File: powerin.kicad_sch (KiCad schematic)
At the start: 12 parts, among them U5 TPS2592xx

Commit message: Add optional ESP32-C3 WiFi sheet, convert hand-solder parts to through-hole
- New wifi sheet: ESP32-C3-MINI-1 module on SPI to spare FPGA bank 34, with EN/boot-strap networks, 3V3 bypass/bulk caps and a UART debug header
- Replace SMD hand-solder resistors, LEDs, zener, fuse and ceramic caps with THT equivalents; bulk 10uF/22uF caps become polarized electrolytics
- Fill in LCSC part numbers for the new parts and regenerate BOM and ERC report
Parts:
- C21: footprint Capacitor_SMD:C_0805_2012Metric_Pad1.18x1.45mm_HandSolder -> Capacitor_THT:CP_Radial_D5.0mm_P2.00mm; symbol Device:C -> Device:C_Polarized; LCSC Part (none) -> C47344176
- C22: footprint Capacitor_SMD:C_0603_1608Metric_Pad1.08x0.95mm_HandSolder -> Capacitor_THT:C_Disc_D3.0mm_W2.0mm_P2.50mm; LCSC Part (none) -> C5632430
- C23: footprint Capacitor_SMD:C_0603_1608Metric_Pad1.08x0.95mm_HandSolder -> Capacitor_THT:C_Disc_D3.0mm_W2.0mm_P2.50mm; LCSC Part (none) -> C1624895
- D2: footprint Diode_SMD:D_SMB_Handsoldering -> Diode_THT:D_DO-41_SOD81_P10.16mm_Horizontal
- F1: footprint Fuse:Fuse_1812_4532Metric_Pad1.30x3.40mm_HandSolder -> easyeda:FUSE-TH_L9.5-W3.5-P5.08-D0.8-S1.2
- R13, R14, R15, R16: footprint Resistor_SMD:R_0603_1608Metric_Pad0.98x0.95mm_HandSolder -> Resistor_THT:R_Axial_DIN0207_L6.3mm_D2.5mm_P10.16mm_Horizontal
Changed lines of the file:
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@@
 			)
 		)
-		(property "Footprint" "Resistor_SMD:R_0603_1608Metric_Pad0.98x0.95mm_HandSolder"
+		(property "Footprint" "Resistor_THT:R_Axial_DIN0207_L6.3mm_D2.5mm_P10.16mm_Horizontal"
 			(at 135.89 31.242 90)
 			(hide yes)
@@
 			)
 		)
-		(property "Footprint" "Resistor_SMD:R_0603_1608Metric_Pad0.98x0.95mm_HandSolder"
+		(property "Footprint" "Resistor_THT:R_Axial_DIN0207_L6.3mm_D2.5mm_P10.16mm_Horizontal"
 			(at 273.812 50.8 90)
 			(hide yes)
@@
 	)
 	(symbol
-		(lib_id "Device:C")
+		(lib_id "Device:C_Polarized")
 		(at 181.61 36.83 0)
 		(unit 1)
@@
 			)
 		)
-		(property "Footprint" "Capacitor_SMD:C_0805_2012Metric_Pad1.18x1.45mm_HandSolder"
+		(property "Footprint" "Capacitor_THT:CP_Radial_D5.0mm_P2.00mm"
 			(at 182.5752 40.64 0)
 			(hide yes)
@@
 		(property "Description" "Unpolarized capacitor"
 			(at 181.61 36.83 0)
+			(hide yes)
+			(show_name no)
+			(do_not_autoplace no)
+			(effects
+				(font
+					(size 1.27 1.27)
+				)
+			)
+		)
+		(property "LCSC Part" "C47344176"
+			(at 0 0 0)
 			(hide yes)
 			(show_name no)
@@
 			)
 		)
-		(property "Footprint" "Capacitor_SMD:C_0603_1608Metric_Pad1.08x0.95mm_HandSolder"
+		(property "Footprint" "Capacitor_THT:C_Disc_D3.0mm_W2.0mm_P2.50mm"
 			(at 266.3952 54.61 0)
 			(hide yes)
@@
 		(property "Description" "Unpolarized capacitor"
 			(at 265.43 50.8 0)
+			(hide yes)
+			(show_name no)
+			(do_not_autoplace no)
+			(effects
+				(font
+					(size 1.27 1.27)
+				)
+			)
+		)
+		(property "LCSC Part" "C1624895"
+			(at 0 0 0)
 			(hide yes)
 			(show_name no)
@@
 			)
 		)
-		(property "Footprint" "Capacitor_SMD:C_0603_1608Metric_Pad1.08x0.95mm_HandSolder"
+		(property "Footprint" "Capacitor_THT:C_Disc_D3.0mm_W2.0mm_P2.50mm"
 			(at 194.0052 40.64 0)
 			(hide yes)
@@
 		(property "Description" "Unpolarized capacitor"
 			(at 193.04 36.83 0)
+			(hide yes)
+			(show_name no)
+			(do_not_autoplace no)
+			(effects
+				(font
+					(size 1.27 1.27)
+				)
+			)
+		)
+		(property "LCSC Part" "C5632430"
+			(at 0 0 0)
 			(hide yes)
 			(show_name no)
@@
 			)
 		)
-		(property "Footprint" "Diode_SMD:D_SMB_Handsoldering"
+		(property "Footprint" "Diode_THT:D_DO-41_SOD81_P10.16mm_Horizontal"
 			(at 44.45 35.56 0)
 			(hide yes)
@@
 			)
 		)
-		(property "Footprint" "Fuse:Fuse_1812_4532Metric_Pad1.30x3.40mm_HandSolder"
+		(property "Footprint" "easyeda:FUSE-TH_L9.5-W3.5-P5.08-D0.8-S1.2"
 			(at 49.53 27.94 0)
 			(hide yes)
@@
 			)
 		)
-		(property "Footprint" "Resistor_SMD:R_0603_1608Metric_Pad0.98x0.95mm_HandSolder"
+		(property "Footprint" "Resistor_THT:R_Axial_DIN0207_L6.3mm_D2.5mm_P10.16mm_Horizontal"
 			(at 135.89 28.702 90)
 			(hide yes)
@@
 			)
 		)
-		(property "Footprint" "Resistor_SMD:R_0603_1608Metric_Pad0.98x0.95mm_HandSolder"
+		(property "Footprint" "Resistor_THT:R_Axial_DIN0207_L6.3mm_D2.5mm_P10.16mm_Horizontal"
 			(at 239.268 38.1 90)
 			(hide yes)

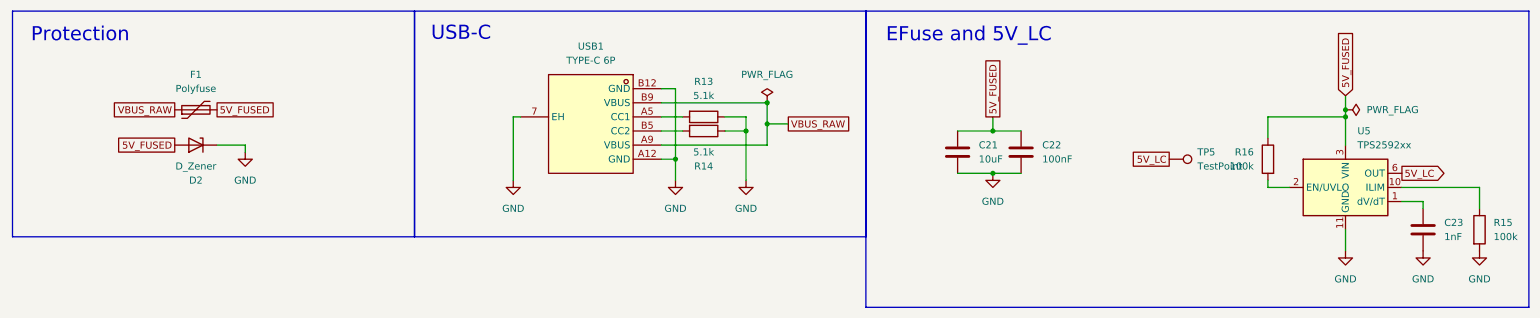
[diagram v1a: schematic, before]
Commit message: Pre-routing checkpoint: zone pours, net labels, decoupling on bottom, R51 1k
- GND pours on F.Cu, In1.Cu, In4.Cu, B.Cu; In3.Cu power pours for 1V0, 1V8,
  5V_LC, MGTAVCC, MGTAVTT, 3V3 (3V3 lowest priority)
- Local labels on previously unnamed power nets
- FPGA decoupling moved to B.Cu under/around U6
- R51 (PUDC_B pull-up) 4.7k -> 1k per UG470
- Silkscreen cleanup
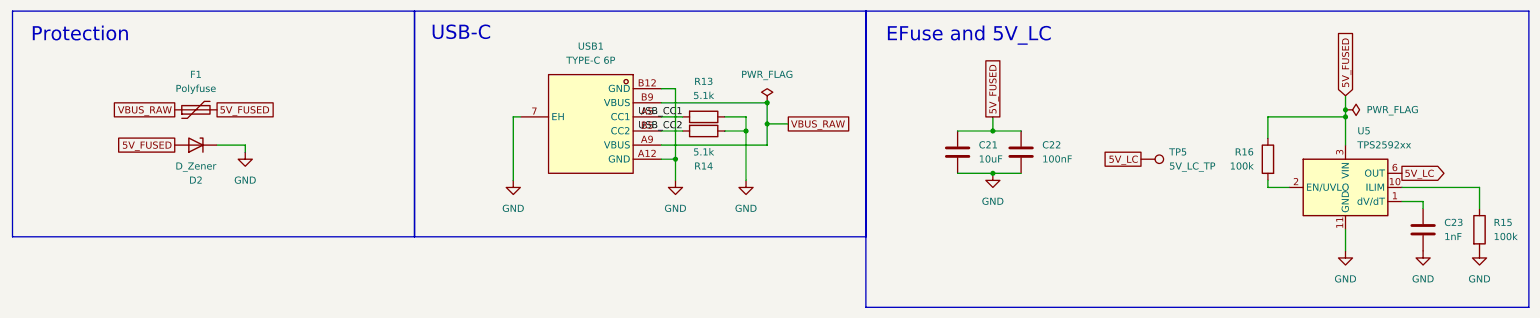
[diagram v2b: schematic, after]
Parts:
- TP5: value TestPoint -> 5V_LC_TP
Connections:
- net USB_CC2: now reaches R14.2, USB1.B5 (CC2)
- net USB_CC1: now reaches R13.2, USB1.A5 (CC1)
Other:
- moved on the sheet: TP5
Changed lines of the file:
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@@
+		)
+	)
+	(label "USB_CC2"
+		(at 132.08 33.02 180)
+		(effects
+			(font
+				(size 1.27 1.27)
+			)
+			(justify right bottom)
+		)
+	)
+	(label "USB_CC1"
+		(at 132.08 30.48 180)
+		(effects
+			(font
+				(size 1.27 1.27)
+			)
+			(justify right bottom)
 		)
 	)
@@
 	(global_label "5V_LC"
 		(shape passive)
-		(at 219.71 38.1 180)
+		(at 214.63 38.1 180)
 		(fields_autoplaced yes)
 		(effects
@@
 		)
 		(property "Intersheetrefs" "${INTERSHEET_REFS}"
-			(at 212.2723 38.1 0)
+			(at 207.1923 38.1 0)
 			(hide yes)
 			(show_name no)
@@
 	(symbol
 		(lib_id "Connector:TestPoint")
-		(at 219.71 38.1 270)
+		(at 214.63 38.1 270)
 		(unit 1)
 		(body_style 1)
@@
 		(fields_autoplaced yes)
 		(property "Reference" "TP5"
-			(at 224.79 36.8299 90)
-			(show_name no)
-			(do_not_autoplace no)
-			(effects
-				(font
-					(size 1.27 1.27)
-				)
-				(justify left)
-			)
-		)
-		(property "Value" "TestPoint"
-			(at 224.79 39.3699 90)
+			(at 219.71 36.8299 90)
+			(show_name no)
+			(do_not_autoplace no)
+			(effects
+				(font
+					(size 1.27 1.27)
+				)
+				(justify left)
+			)
+		)
+		(property "Value" "5V_LC_TP"
+			(at 219.71 39.3699 90)
 			(show_name no)
 			(do_not_autoplace no)
@@
 		)
 		(property "Footprint" "TestPoint:TestPoint_THTPad_D1.5mm_Drill0.7mm"
-			(at 219.71 43.18 0)
+			(at 214.63 43.18 0)
 			(hide yes)
 			(show_name no)
@@
 		)
 		(property "Datasheet" ""
-			(at 219.71 43.18 0)
+			(at 214.63 43.18 0)
 			(hide yes)
 			(show_name no)
@@
 		)
 		(property "Description" "test point"
-			(at 219.71 38.1 0)
-			(hide yes)
-			(show_name no)
+			(at 214.63 38.1 0)
+			(hide yes)
+			(show_name no)
